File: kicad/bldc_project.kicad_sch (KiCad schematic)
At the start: 0 parts

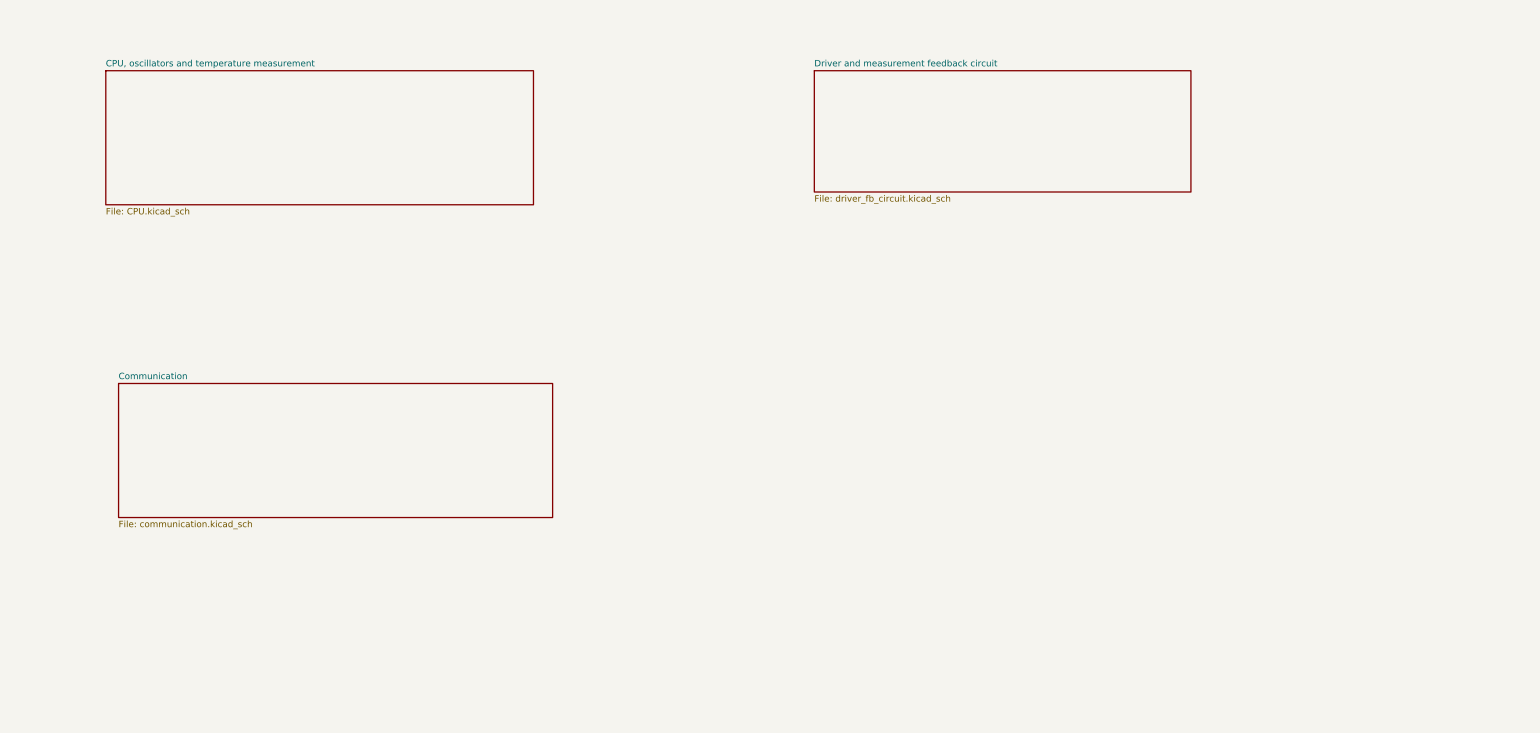
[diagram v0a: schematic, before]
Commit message: [kicad] added soldering pads for phases and battery connectors, rearranged schematic, added tooling holes, fixed ERC errors [scripts] minor footprint calculations
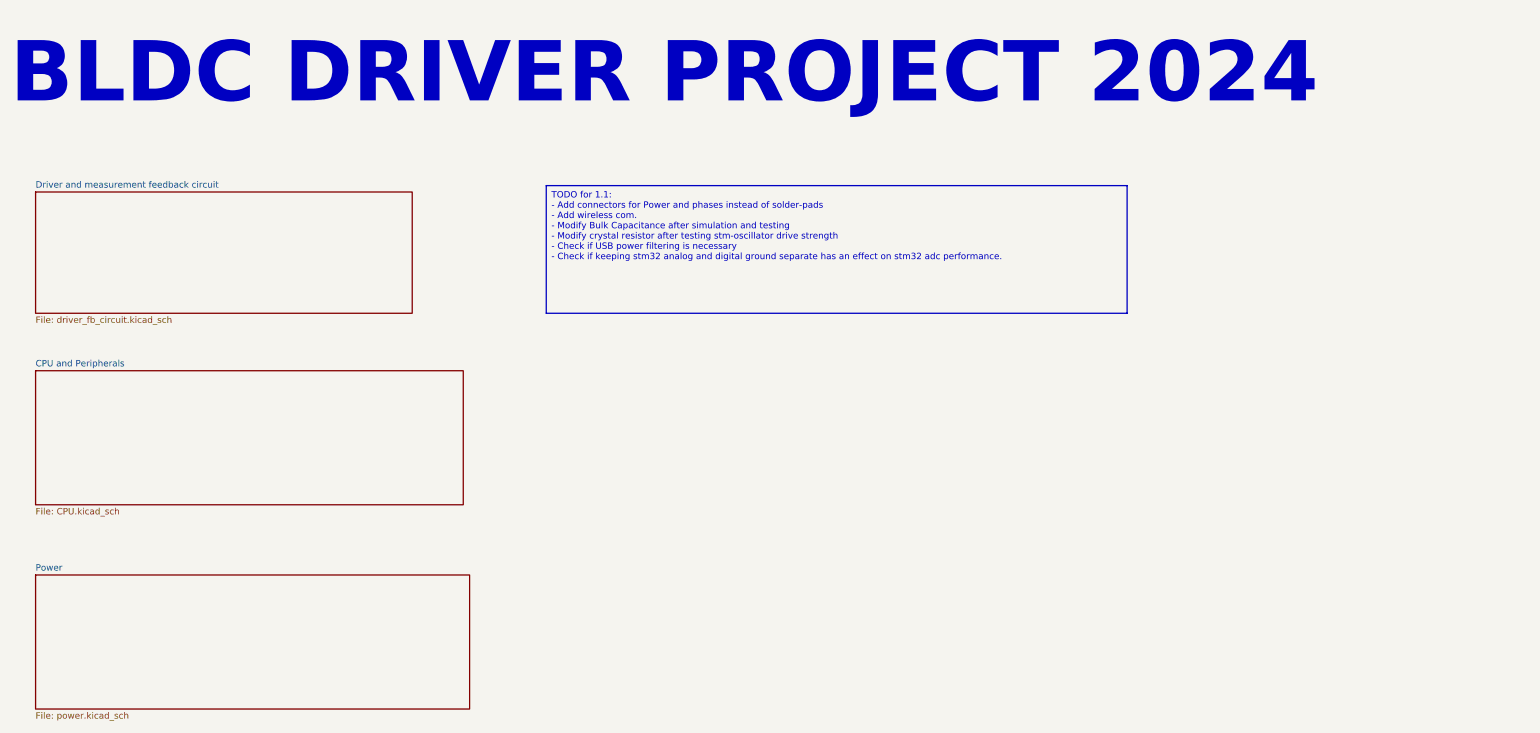
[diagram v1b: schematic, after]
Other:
- sheet CPU, oscillators and temperature measurement renamed CPU and Peripherals
- sheet Communication renamed Power
- sheet Power: file communication.kicad_sch -> power.kicad_sch
- note added: "BLDC DRIVER PROJECT 2024"
- company: (none) -> Igor Wolfs
- title: (none) -> BLDC Driver Project
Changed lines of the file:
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@@
 (kicad_sch (version 20230121) (generator eeschema)
   (paper "A4")
-  (sheet (at 39.37 88.9) (size 86.36 26.67) (fields_autoplaced)
+  (title_block
+    (title "BLDC Driver Project")
+    (rev "1.0")
+    (company "Igor Wolfs")
+    (comment 1 "fsad")
+  )
+  (text_box "TODO for 1.1:\n- Add connectors for Power and phases instead of solder-pads\n- Add wireless com.\n- Modify Bulk Capacitance after simulation and testing\n- Modify crystal resistor after testing stm-oscillator drive strength\n- Check if USB power filtering is necessary\n- Check if keeping stm32 analog and digital ground separate has an effect on stm32 adc performance."
+    (at 124.46 49.53 0) (size 115.57 25.4)
+    (stroke (width 0) (type default))
+    (fill (type none))
+    (effects (font (size 1.27 1.27)) (justify left top))
+  )
+  (text "BLDC DRIVER PROJECT 2024" (at 17.78 34.29 0)
+    (effects (font (size 12 12) (thickness 2.4) bold) (justify left bottom))
+  )
+  (sheet (at 22.86 127) (size 86.36 26.67) (fields_autoplaced)
     (stroke (width 0.1524) (type solid))
     (fill (color 0 0 0 0.0000))
-    (property "Sheetname" "Communication" (at 39.37 88.1884 0)
+    (property "Sheetname" "Power" (at 22.86 126.2884 0)
       (effects (font (size 1.27 1.27)) (justify left bottom))
     )
-    (property "Sheetfile" "communication.kicad_sch" (at 39.37 116.1546 0)
+    (property "Sheetfile" "power.kicad_sch" (at 22.86 154.2546 0)
       (effects (font (size 1.27 1.27)) (justify left top))
     )
@@
     )
   )
-  (sheet (at 36.83 26.67) (size 85.09 26.67) (fields_autoplaced)
+  (sheet (at 22.86 86.36) (size 85.09 26.67) (fields_autoplaced)
     (stroke (width 0.1524) (type solid))
     (fill (color 0 0 0 0.0000))
-    (property "Sheetname" "CPU, oscillators and temperature measurement" (at 36.83 25.9584 0)
+    (property "Sheetname" "CPU and Peripherals" (at 22.86 85.6484 0)
       (effects (font (size 1.27 1.27)) (justify left bottom))
     )
-    (property "Sheetfile" "CPU.kicad_sch" (at 36.83 53.9246 0)
+    (property "Sheetfile" "CPU.kicad_sch" (at 22.86 113.6146 0)
       (effects (font (size 1.27 1.27)) (justify left top))
     )
@@
     )
   )
-  (sheet (at 177.8 26.67) (size 74.93 24.13) (fields_autoplaced)
+  (sheet (at 22.86 50.8) (size 74.93 24.13) (fields_autoplaced)
     (stroke (width 0.1524) (type solid))
     (fill (color 0 0 0 0.0000))
-    (property "Sheetname" "Driver and measurement feedback circuit" (at 177.8 25.9584 0)
+    (property "Sheetname" "Driver and measurement feedback circuit" (at 22.86 50.0884 0)
       (effects (font (size 1.27 1.27)) (justify left bottom))
     )
-    (property "Sheetfile" "driver_fb_circuit.kicad_sch" (at 177.8 51.3846 0)
+    (property "Sheetfile" "driver_fb_circuit.kicad_sch" (at 22.86 75.5146 0)
       (effects (font (size 1.27 1.27)) (justify left top))
     )

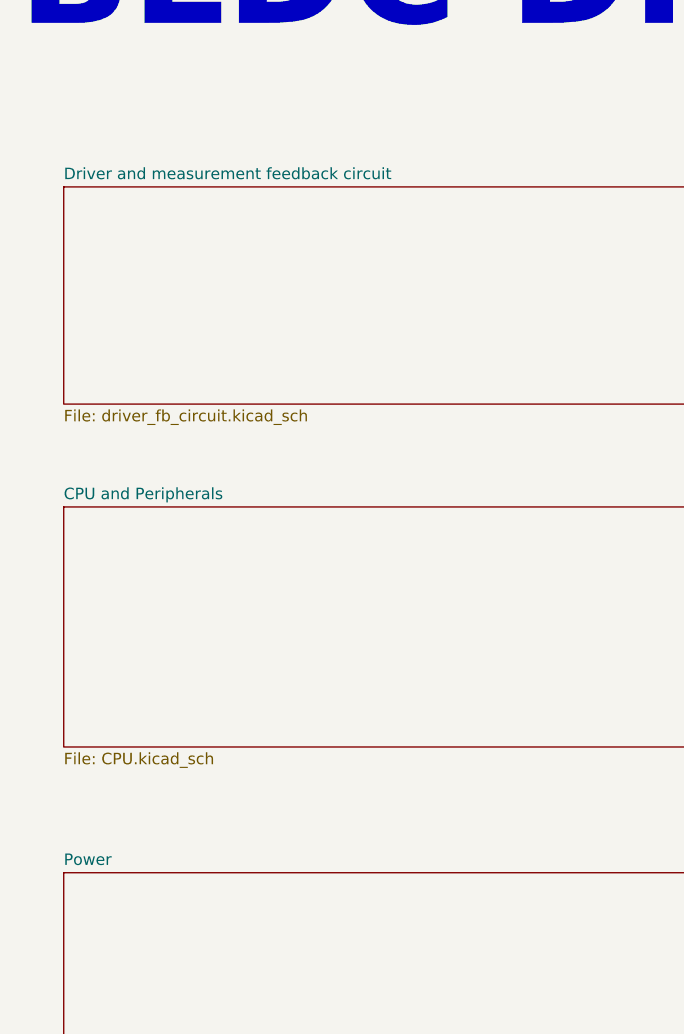
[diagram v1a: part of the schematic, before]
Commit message: [bldc] Fixed footprint issues, added jlcpcb man. rules, stackup decisions, added nets..
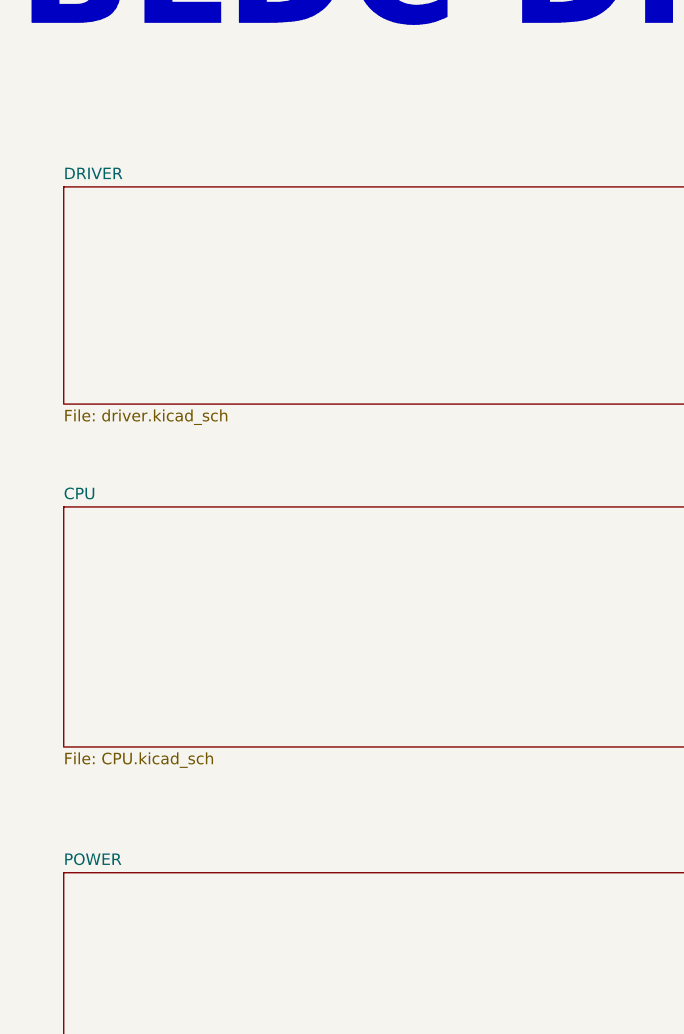
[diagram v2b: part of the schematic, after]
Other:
- sheet CPU and Peripherals renamed CPU
- sheet Driver and measurement feedback circuit renamed DRIVER
- sheet Power renamed POWER
- sheet DRIVER: file driver_fb_circuit.kicad_sch -> driver.kicad_sch
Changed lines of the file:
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@@
     (stroke (width 0.1524) (type solid))
     (fill (color 0 0 0 0.0000))
-    (property "Sheetname" "Power" (at 22.86 126.2884 0)
+    (property "Sheetname" "POWER" (at 22.86 126.2884 0)
       (effects (font (size 1.27 1.27)) (justify left bottom))
     )
@@
     (stroke (width 0.1524) (type solid))
     (fill (color 0 0 0 0.0000))
-    (property "Sheetname" "CPU and Peripherals" (at 22.86 85.6484 0)
+    (property "Sheetname" "CPU" (at 22.86 85.6484 0)
       (effects (font (size 1.27 1.27)) (justify left bottom))
     )
@@
     (stroke (width 0.1524) (type solid))
     (fill (color 0 0 0 0.0000))
-    (property "Sheetname" "Driver and measurement feedback circuit" (at 22.86 50.0884 0)
+    (property "Sheetname" "DRIVER" (at 22.86 50.0884 0)
       (effects (font (size 1.27 1.27)) (justify left bottom))
     )
-    (property "Sheetfile" "driver_fb_circuit.kicad_sch" (at 22.86 75.5146 0)
+    (property "Sheetfile" "driver.kicad_sch" (at 22.86 75.5146 0)
       (effects (font (size 1.27 1.27)) (justify left top))
     )

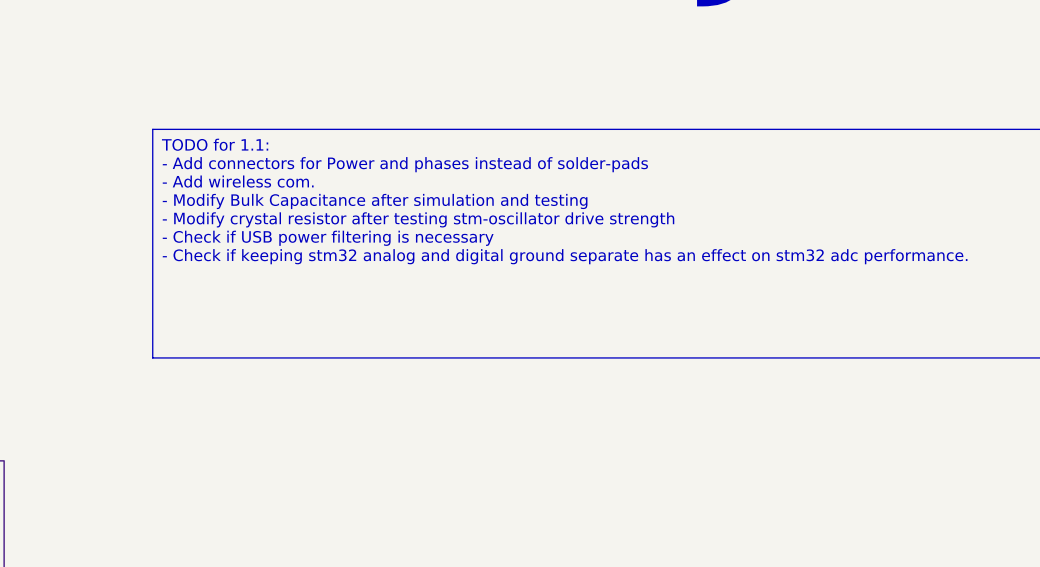
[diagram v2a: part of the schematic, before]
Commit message: [kicad] positioning of single inverter stage
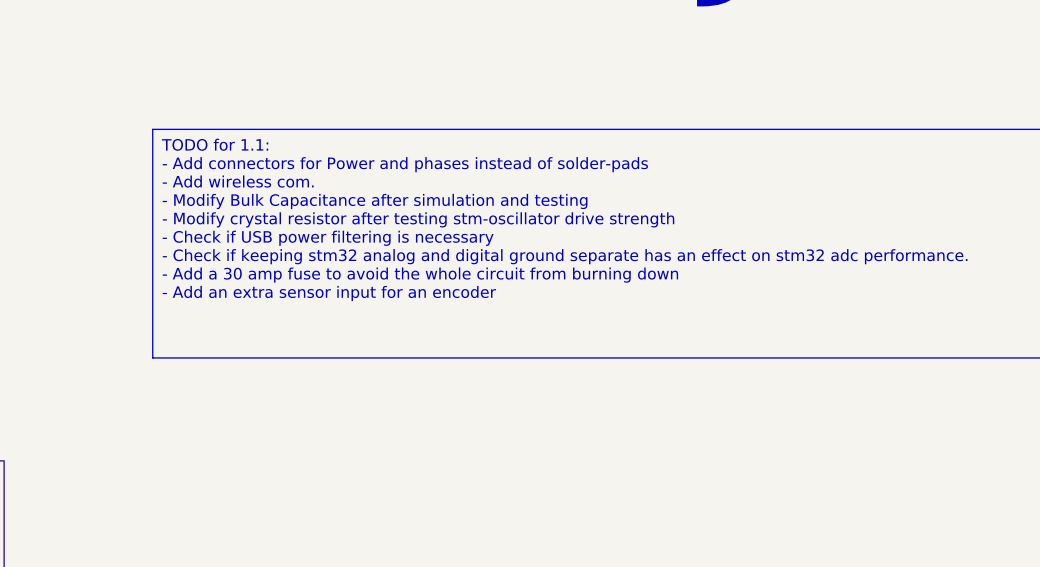
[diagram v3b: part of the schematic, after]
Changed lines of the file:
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@@
     (comment 1 "fsad")
   )
-  (text_box "TODO for 1.1:\n- Add connectors for Power and phases instead of solder-pads\n- Add wireless com.\n- Modify Bulk Capacitance after simulation and testing\n- Modify crystal resistor after testing stm-oscillator drive strength\n- Check if USB power filtering is necessary\n- Check if keeping stm32 analog and digital ground separate has an effect on stm32 adc performance."
+  (text_box "TODO for 1.1:\n- Add connectors for Power and phases instead of solder-pads\n- Add wireless com.\n- Modify Bulk Capacitance after simulation and testing\n- Modify crystal resistor after testing stm-oscillator drive strength\n- Check if USB power filtering is necessary\n- Check if keeping stm32 analog and digital ground separate has an effect on stm32 adc performance.\n- Add a 30 amp fuse to avoid the whole circuit from burning down\n- Add an extra sensor input for an encoder"
     (at 124.46 49.53 0) (size 115.57 25.4)
     (stroke (width 0) (type default))

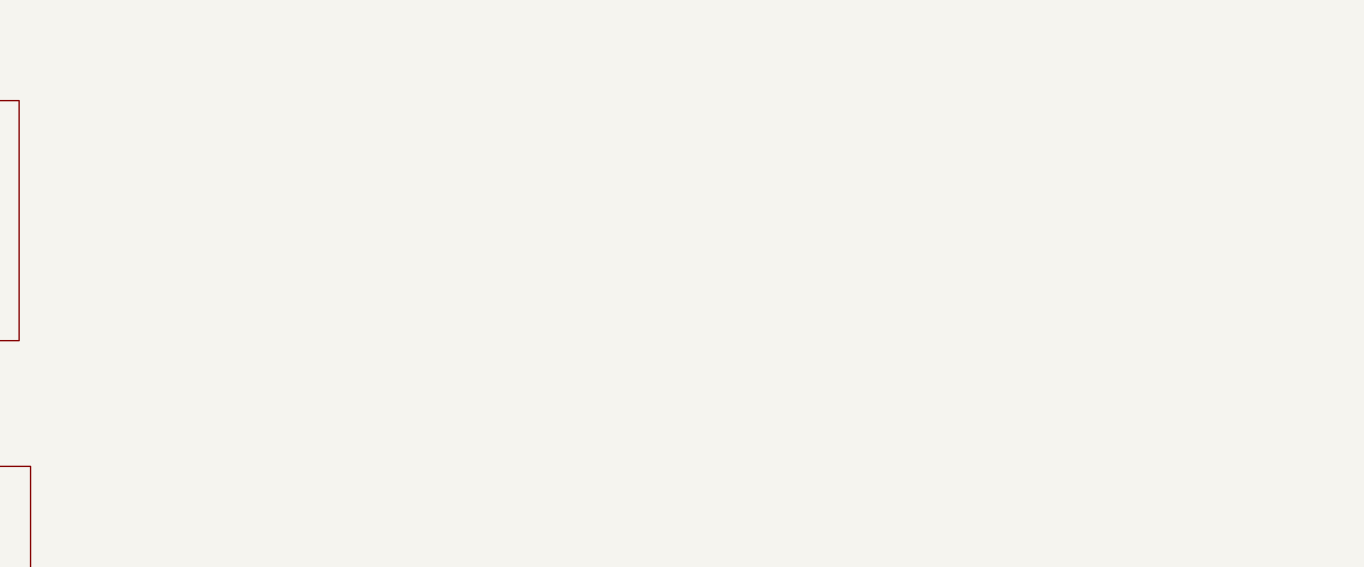
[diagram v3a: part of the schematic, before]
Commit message: [kicad] changed some footprints | TODO: Fix footprint of USB-ESD protection, recheck components, fix ERC errors
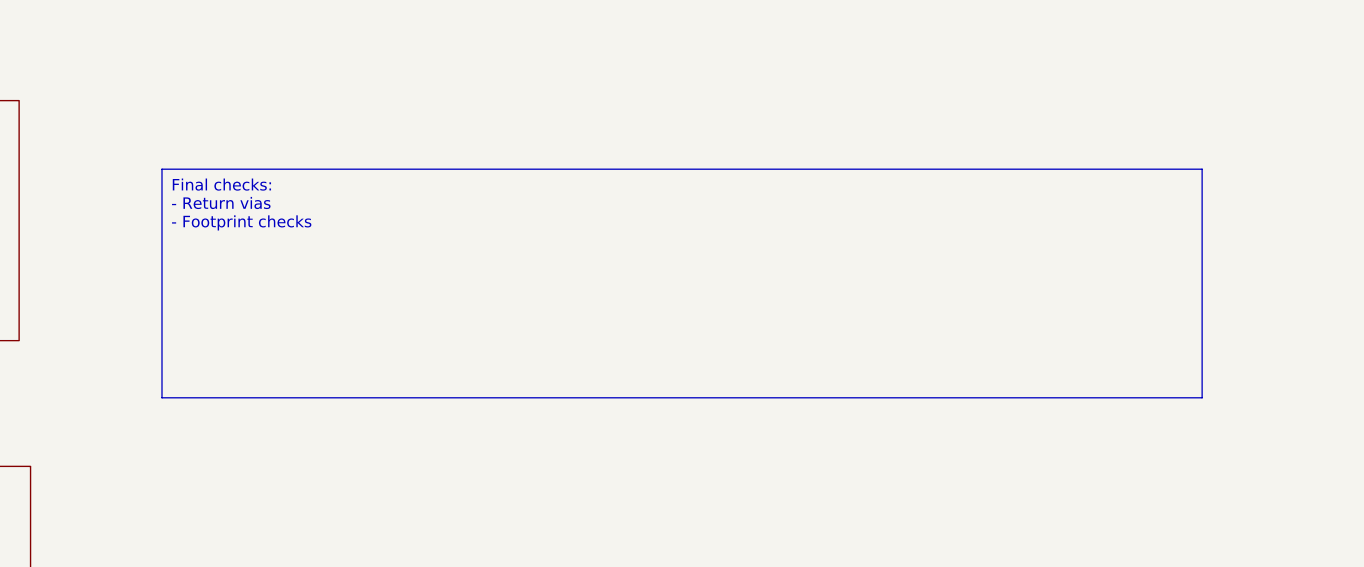
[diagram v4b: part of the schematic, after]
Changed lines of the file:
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@@
     (comment 1 "fsad")
+  )
+  (text_box "Final checks:\n- Return vias\n- Footprint checks\n"
+    (at 123.825 93.98 0) (size 115.57 25.4)
+    (stroke (width 0) (type default))
+    (fill (type none))
+    (effects (font (size 1.27 1.27)) (justify left top))
   )
   (text_box "TODO for 1.1:\n- Add connectors for Power and phases instead of solder-pads\n- Add wireless com.\n- Modify Bulk Capacitance after simulation and testing\n- Modify crystal resistor after testing stm-oscillator drive strength\n- Check if USB power filtering is necessary\n- Check if keeping stm32 analog and digital ground separate has an effect on stm32 adc performance.\n- Add a 30 amp fuse to avoid the whole circuit from burning down\n- Add an extra sensor input for an encoder"
